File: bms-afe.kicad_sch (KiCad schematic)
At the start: 13 parts, among them J1 CONN HEADER VERT 7POS 2.5MM

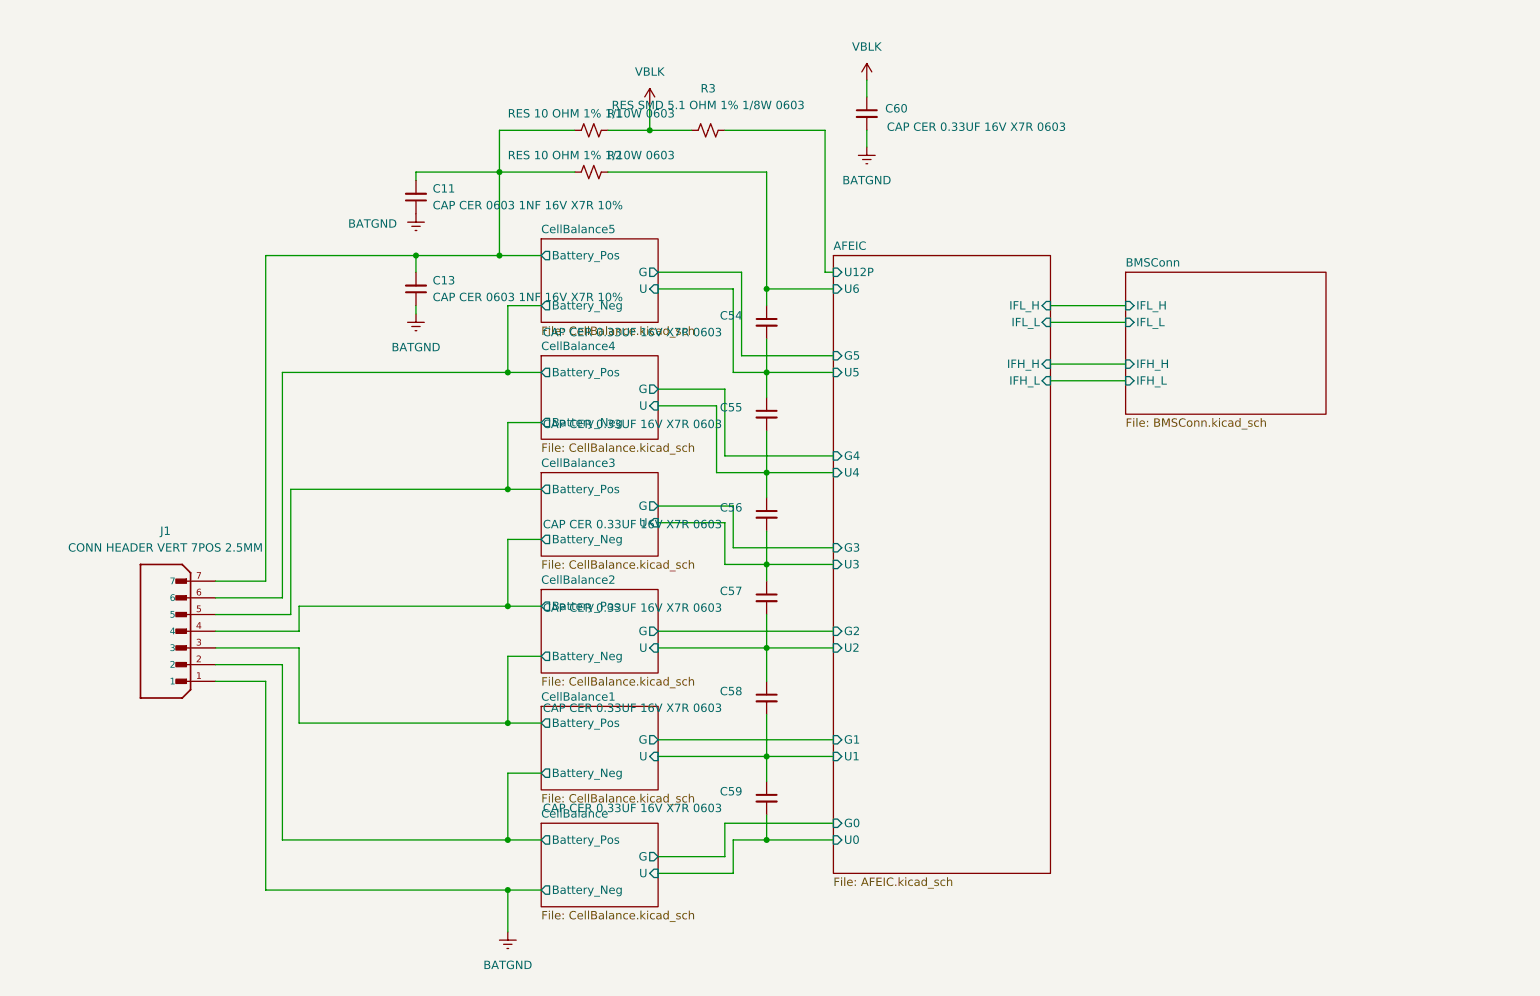
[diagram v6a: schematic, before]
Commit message: cleaned up schematic
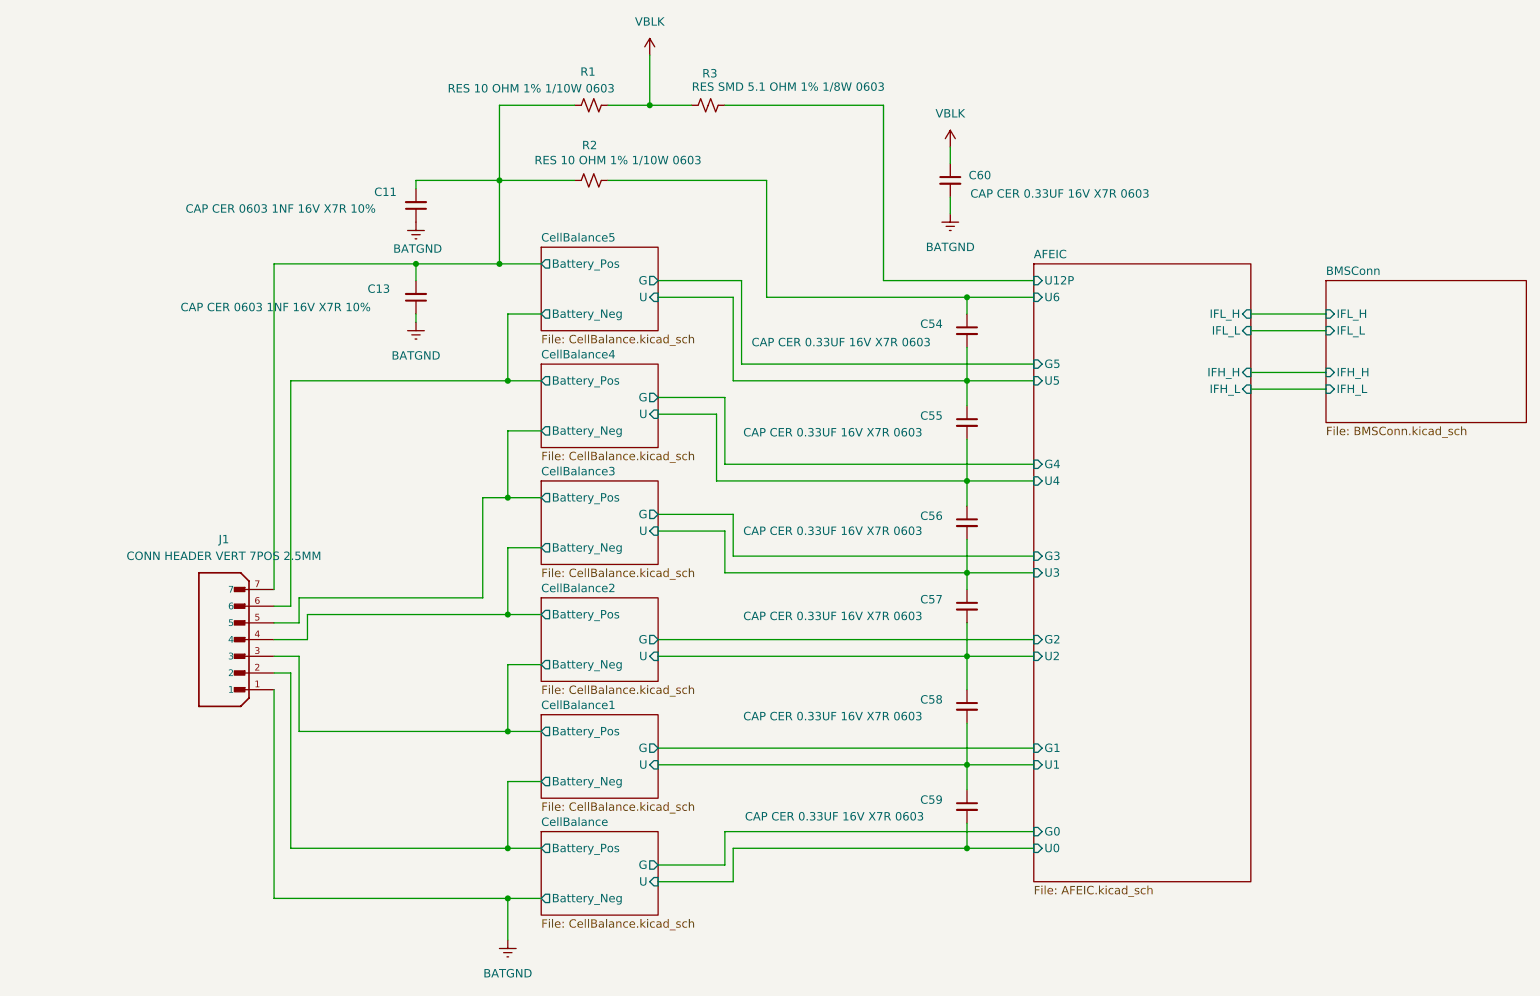
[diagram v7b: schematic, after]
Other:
- moved on the sheet: C11, C13, C54, C55, C56, C57, C58, C59, C60, J1, R1, R2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

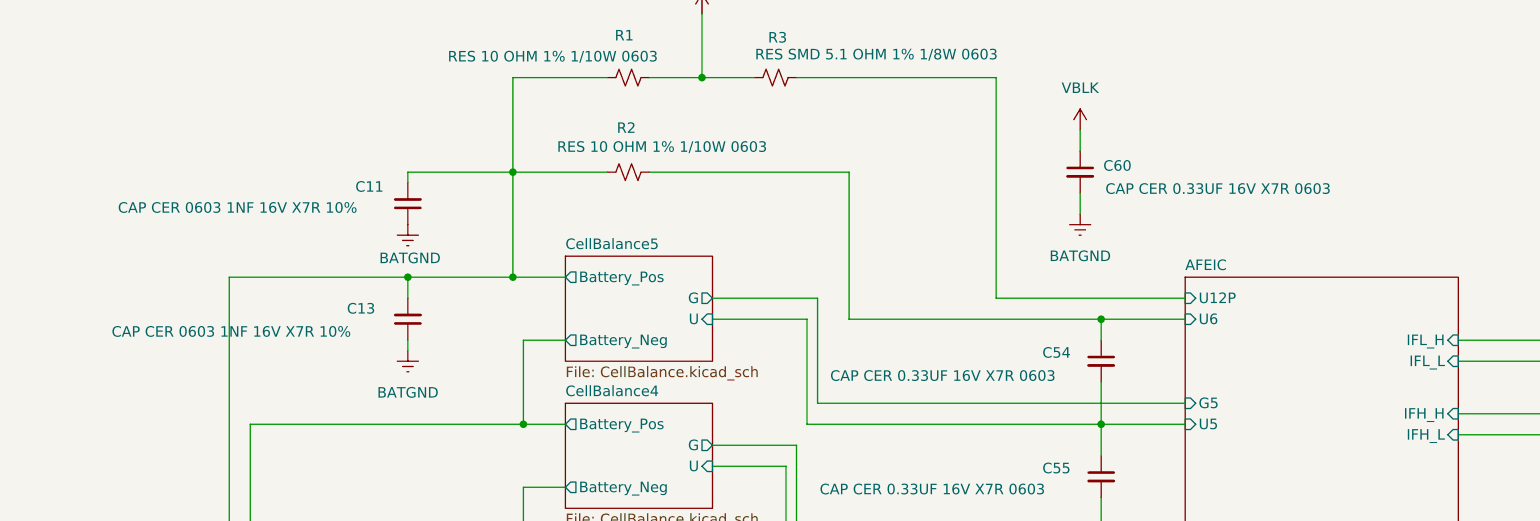
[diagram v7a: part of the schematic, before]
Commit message: fixed capacitor values
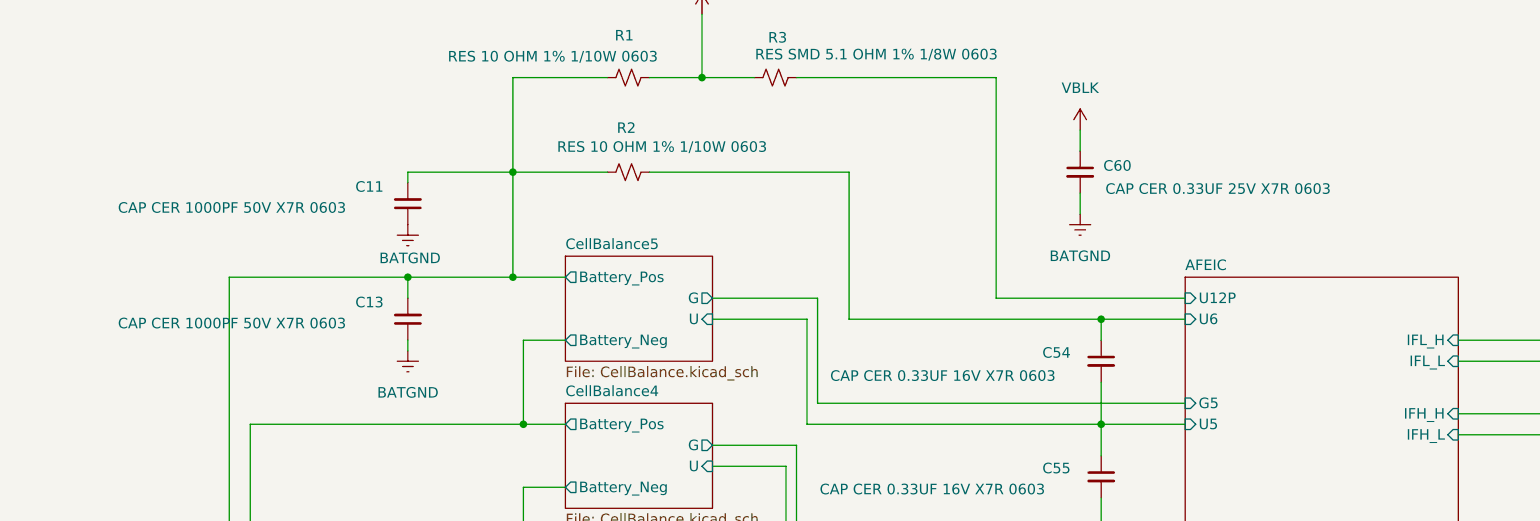
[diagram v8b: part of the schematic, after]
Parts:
- C11, C13: value CAP CER 0603 1NF 16V X7R 10% -> CAP CER 1000PF 50V X7R 0603
- C60: value CAP CER 0.33UF 16V X7R 0603 -> CAP CER 0.33UF 25V X7R 0603
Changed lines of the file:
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@@
+	(symbol
+		(lib_id "Device:C_Small")
+		(at 102.87 60.96 180)
+		(unit 1)
+		(body_style 1)
+		(exclude_from_sim no)
+		(in_bom yes)
+		(on_board yes)
+		(in_pos_files yes)
+		(dnp no)
+		(property "Reference" "C13"
+			(at 96.52 58.928 0)
+			(show_name no)
+			(do_not_autoplace no)
+			(effects
+				(font
+					(size 1.27 1.27)
+				)
+				(justify right)
+			)
+		)
+		(property "Value" "CAP CER 1000PF 50V X7R 0603"
+			(at 67.818 61.468 0)
+			(show_name no)
+			(do_not_autoplace no)
+			(effects
+				(font
+					(size 1.27 1.27)
+				)
+				(justify right)
+			)
+		)
+		(property "Footprint" "Capacitor_SMD:C_0603_1608Metric"
+			(at 102.87 60.96 0)
+			(hide yes)
+			(show_name no)
+			(do_not_autoplace no)
+			(effects
+				(font
+					(size 1.27 1.27)
+				)
+			)
+		)
+		(property "Datasheet" "https://www.digikey.ca/en/products/detail/samsung-electro-mechanics/CL10B102KB8NNNC/3886676"
+			(at 102.87 60.96 0)
+			(hide yes)
+			(show_name no)
+			(do_not_autoplace no)
+			(effects
+				(font
+					(size 1.27 1.27)
+				)
+			)
+		)
+		(property "Description" "1000 pF ±10% 50V Ceramic Capacitor X7R 0603 (1608 Metric)"
+			(at 102.87 60.96 0)
+			(hide yes)
+			(show_name no)
+			(do_not_autoplace no)
+			(effects
+				(font
+					(size 1.27 1.27)
+				)
+			)
+		)
+		(pin "2"
+		)
+		(pin "1"
+		)
+		(instances
+			(project "bms-afe"
+				(path "/226a23e7-09bb-40bc-b53a-ec42a6b7cc90"
+					(reference "C13")
+					(unit 1)
+				)
+			)
+		)
+	)
 	(symbol
 		(lib_id "Device:C_Small")
@@
 			)
 		)
-		(property "Value" "CAP CER 0603 1NF 16V X7R 10%"
+		(property "Value" "CAP CER 1000PF 50V X7R 0603"
 			(at 67.818 47.498 0)
 			(show_name no)
@@
 			)
 		)
-		(property "Datasheet" "https://www.digikey.ca/en/products/detail/kemet/C0603C102K4RECAUTO/8640472"
+		(property "Datasheet" "https://www.digikey.ca/en/products/detail/samsung-electro-mechanics/CL10B102KB8NNNC/3886676"
 			(at 102.87 46.99 0)
 			(hide yes)
@@
 			)
 		)
-		(property "Description" "1000 pF ±10% 16V Ceramic Capacitor X7R 0603 (1608 Metric)"
+		(property "Description" "1000 pF ±10% 50V Ceramic Capacitor X7R 0603 (1608 Metric)"
 			(at 102.87 46.99 0)
 			(hide yes)
@@
 			)
 		)
-		(property "Value" "CAP CER 0.33UF 16V X7R 0603"
+		(property "Value" "CAP CER 0.33UF 25V X7R 0603"
 			(at 187.198 45.212 0)
 			(show_name no)
@@
 			)
 		)
-		(property "Datasheet" "https://www.digikey.ca/en/products/detail/samsung-electro-mechanics/CL10B334KO8NNNC/3887706"
+		(property "Datasheet" "https://www.digikey.ca/en/products/detail/w%C3%BCrth-elektronik/885012206074/5453847"
 			(at 184.15 43.18 0)
 			(hide yes)
@@
 			)
 		)
-		(property "Description" "0.33 µF ±10% 16V Ceramic Capacitor X7R 0603 (1608 Metric)"
+		(property "Description" "0.33 µF ±10% 25V Ceramic Capacitor X7R 0603 (1608 Metric)"
 			(at 184.15 43.18 0)
 			(hide yes)
@@
 					(unit 1)
 				)
-			)
-		)
-	)
-	(symbol
-		(lib_id "Device:C_Small")
-		(at 102.87 60.96 180)
-		(unit 1)
-		(body_style 1)
-		(exclude_from_sim no)
-		(in_bom yes)
-		(on_board yes)
-		(in_pos_files yes)
-		(dnp no)
-		(property "Reference" "C13"
-			(at 95.504 59.69 0)
-			(show_name no)
-			(do_not_autoplace no)
-			(effects
-				(font
-					(size 1.27 1.27)
-				)
-				(justify right)
-			)
-		)
-		(property "Value" "CAP CER 0603 1NF 16V X7R 10%"
-			(at 67.056 62.484 0)
-			(show_name no)
-			(do_not_autoplace no)
-			(effects
-				(font
-					(size 1.27 1.27)
-				)
-				(justify right)
-			)
-		)
-		(property "Footprint" "Capacitor_SMD:C_0603_1608Metric"
-			(at 102.87 60.96 0)
-			(hide yes)
-			(show_name no)
-			(do_not_autoplace no)
-			(effects
-				(font
-					(size 1.27 1.27)
-				)
-			)
-		)
-		(property "Datasheet" "https://www.digikey.ca/en/products/detail/kemet/C0603C102K4RECAUTO/8640472"
-			(at 102.87 60.96 0)
-			(hide yes)
-			(show_name no)
-			(do_not_autoplace no)
-			(effects
-				(font
-					(size 1.27 1.27)
-				)
-			)
-		)
-		(property "Description" "1000 pF ±10% 16V Ceramic Capacitor X7R 0603 (1608 Metric)"
-			(at 102.87 60.96 0)
-			(hide yes)
-			(show_name no)
-			(do_not_autoplace no)
-			(effects
-				(font
-					(size 1.27 1.27)
-				)
-			)
-		)
-		(pin "2"
-		)
-		(pin "1"
-		)
-		(instances
-			(project "bms-afe"
-				(path "/226a23e7-09bb-40bc-b53a-ec42a6b7cc90"
-					(reference "C13")
-					(unit 1)
-				)
